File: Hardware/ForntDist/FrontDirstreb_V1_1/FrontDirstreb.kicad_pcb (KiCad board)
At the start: 2 copper layers, 69 x 25 mm, 19 parts, among them J1 Banana, J2 Banana, J3 Banana, J4 Banana, J5 Earth, J6 Sense, J7 LED, J8 Power, J9 Earth

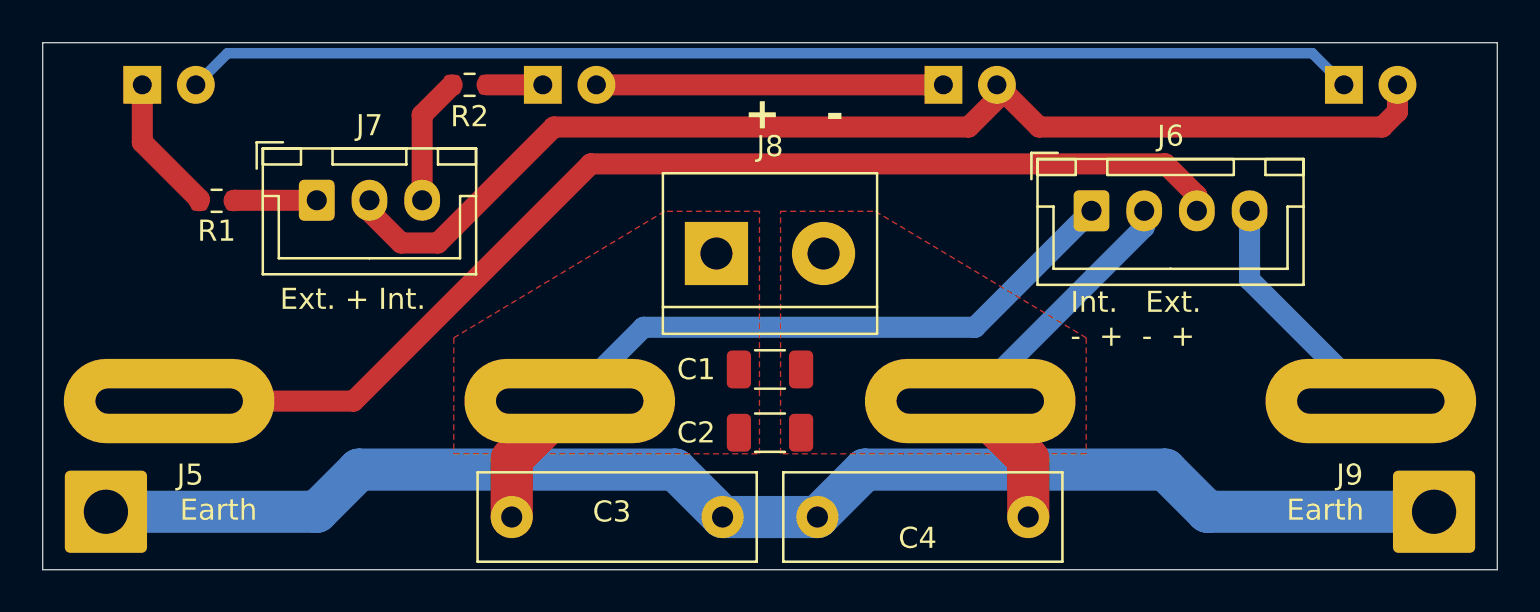
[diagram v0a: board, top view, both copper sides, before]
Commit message: rooting and new frontDist
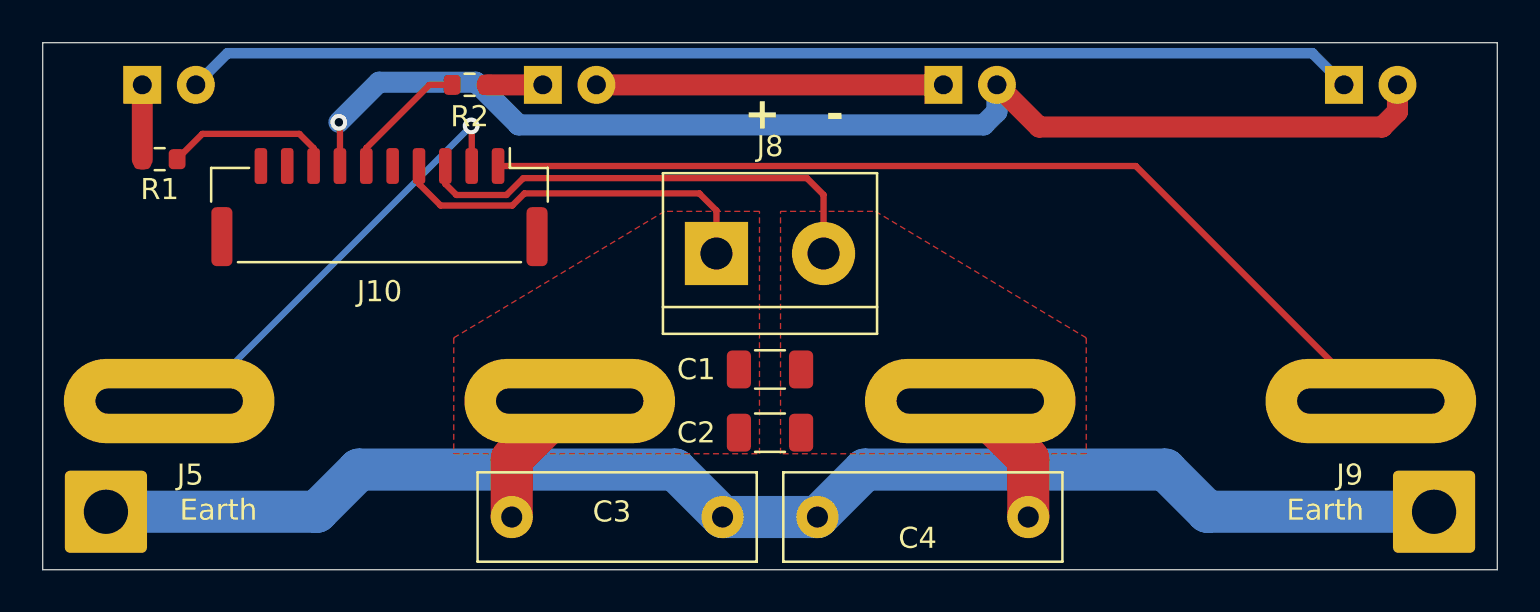
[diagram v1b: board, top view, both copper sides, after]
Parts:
- removed J6: Sense, Connector_JST:JST_XH_B4B-XH-A_1x04_P2.50mm_Vertical
- removed J7: LED, Connector_JST:JST_XH_B3B-XH-A_1x03_P2.50mm_Vertical
- added J10: Conn_01x10_Socket, Connector_JST:JST_GH_BM10B-GHS-TBT_1x10-1MP_P1.25mm_Vertical, F.Cu at (132.5, 86.3)
- moved R1 3.35 mm to (122.0, 84.0)
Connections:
- net Net-(D3-A) renamed +5V
- J1 pad 1: Net-(J1-Pin_1) -> /ExSense-
- J4 pad 1: Net-(J4-Pin_1) -> /ExSense+
- R1 pad 1: Net-(J7-Pin_1) -> /LED_SenseEx
- R2 pad 1: Net-(J7-Pin_3) -> /LED_ON
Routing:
- net Net-(J1-Pin_1): track 54.8 -> 0.00 mm
- net /ExSense+: track 0.00 -> 46.0 mm
- net /ExSense-: track 0.00 -> 21.6 mm, vias 0 -> 1
- net Net-(J4-Pin_1): track 11.4 -> 0.00 mm
- net /Ch1Pw-: track 35.1 -> 24.6 mm
- net /Ch1Pw+: track 19.1 -> 29.1 mm
- net /LED_SenseEx: track 0.00 -> 8.10 mm
- net /LED_ON: track 0.00 -> 6.17 mm
- net Net-(J7-Pin_3): track 6.07 -> 0.00 mm
- net Net-(J7-Pin_1): track 3.94 -> 0.00 mm
- net Net-(D1-K): track 6.62 -> 3.53 mm
- net +5V: track 55.8 -> 57.9 mm, vias 0 -> 1
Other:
- board text removed: "Ext. + Int."
- board text removed: "Int. Ext. - + - +"
